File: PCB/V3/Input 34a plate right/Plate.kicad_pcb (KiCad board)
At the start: 2 copper layers, 109.9 x 100.3 mm, 22 parts, among them SW1 SW_Push, SW10 SW_Push, SW11 SW_Push, SW13 SW_Push, SW14 SW_Push, SW15 SW_Push, SW16 SW_Push, SW17 SW_Push, SW2 SW_Push, SW22 SW_Push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

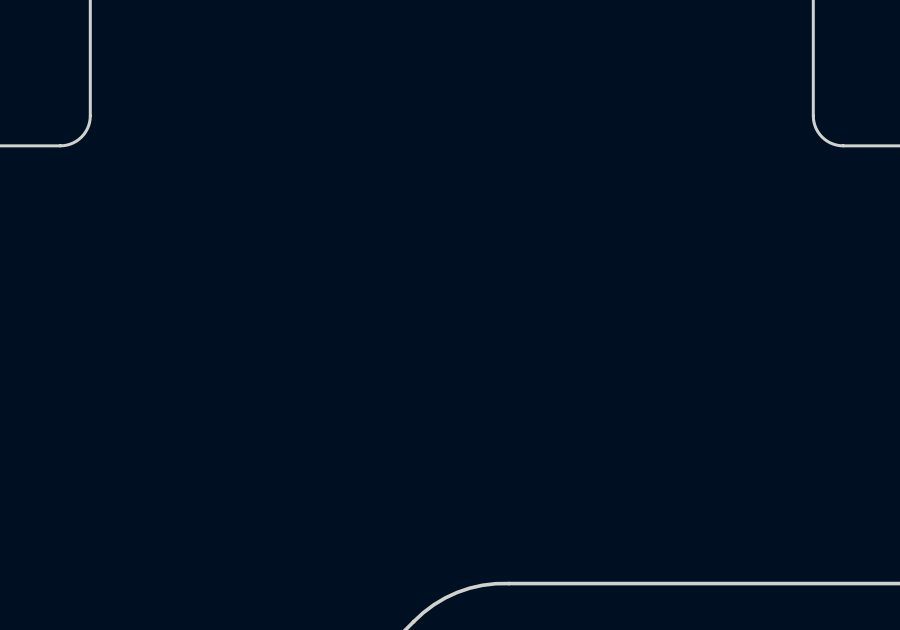
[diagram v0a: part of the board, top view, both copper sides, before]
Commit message: update logo
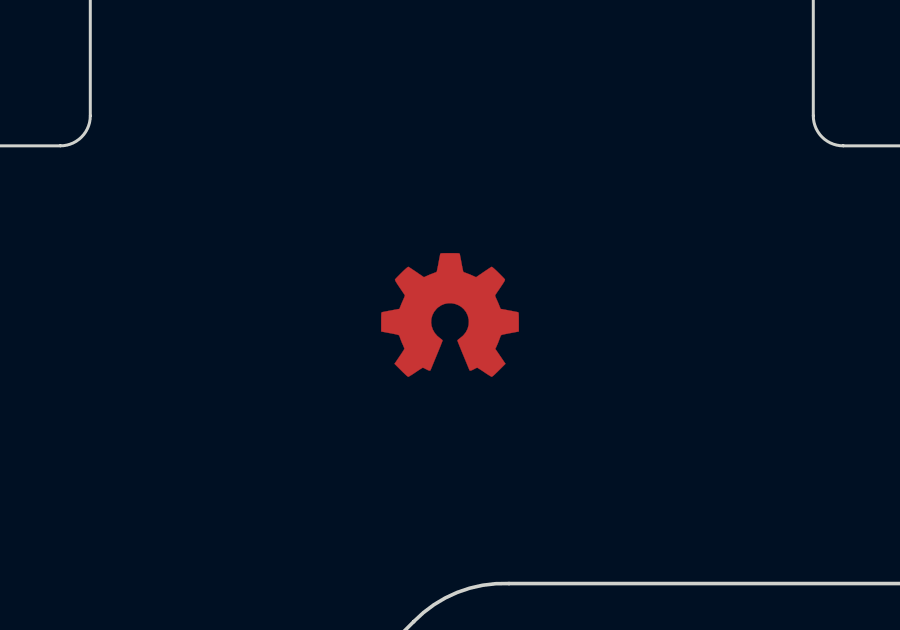
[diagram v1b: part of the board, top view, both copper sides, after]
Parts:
- removed the REF** at (105.4, 117.5)
- added REF**: OSHW-Logo2_5x5mm_Copper, Keyboard_JSA:OSHW-Logo2_5x5mm_Copper, F.Cu at (105.4, 118.1)
